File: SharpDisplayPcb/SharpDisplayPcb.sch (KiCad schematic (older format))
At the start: 1 part, among them J1 Conn_01x08_Female

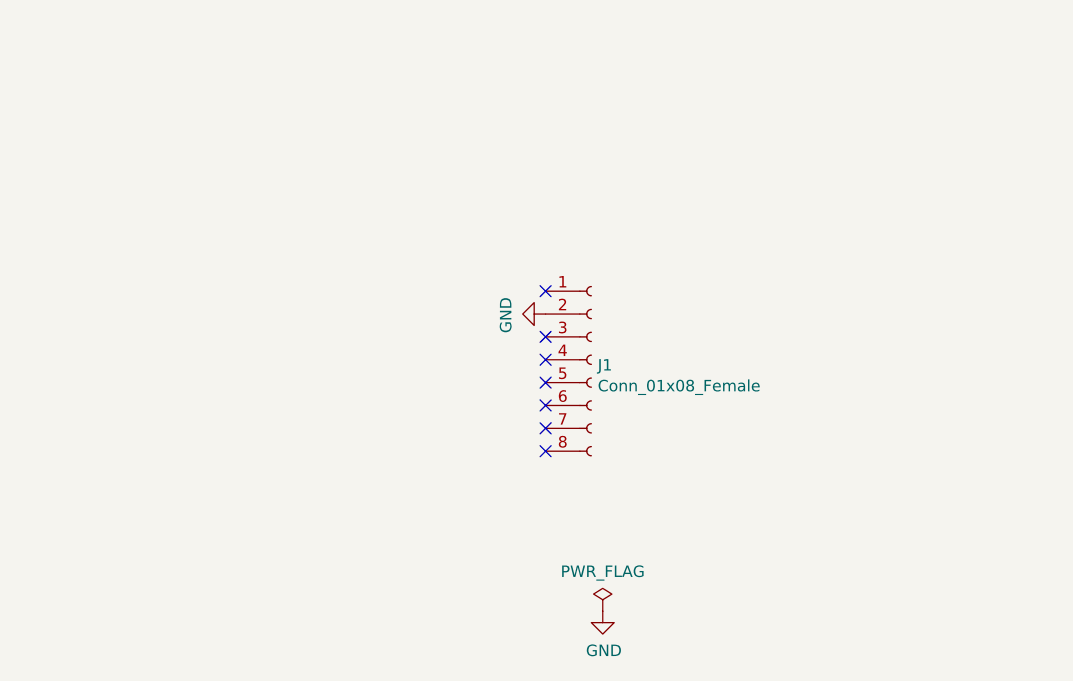
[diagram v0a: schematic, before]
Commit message: Completed schematics, initial PCB layout
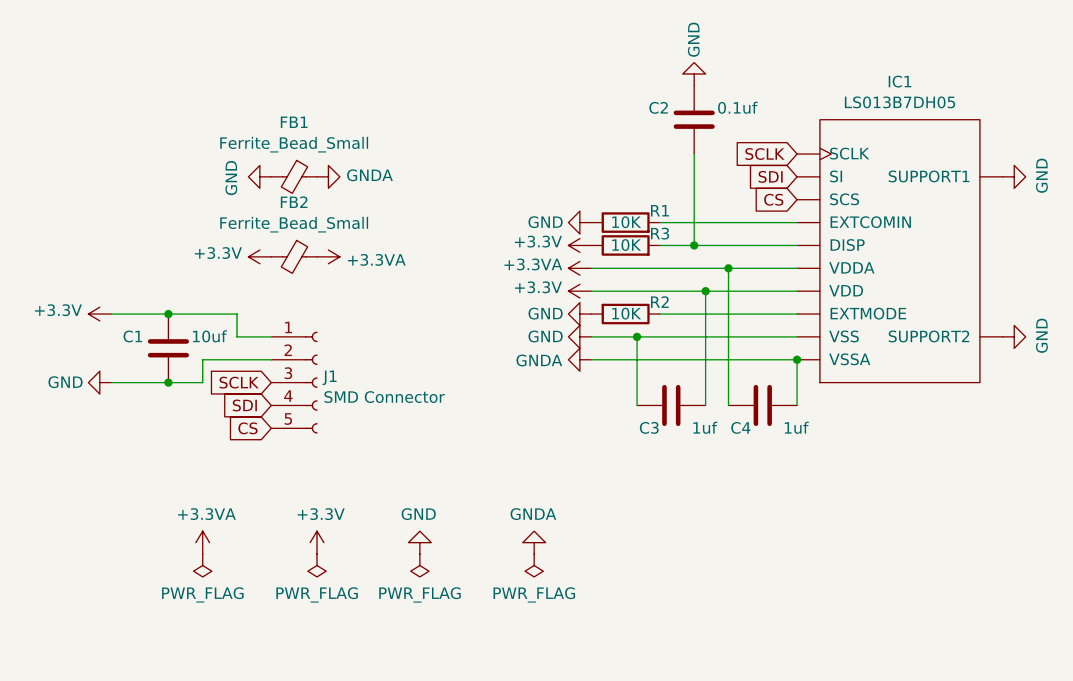
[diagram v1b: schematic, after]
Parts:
- removed J1: Conn_01x08_Female, Connector_PinHeader_2.54mm:PinHeader_1x08_P2.54mm_Vertical, symbol Connector:Conn_01x08_Female
- added C1: 10uf, Capacitor_SMD:C_0805_2012Metric_Pad1.18x1.45mm_HandSolder, symbol Device:C
- added C2: 0.1uf, Capacitor_SMD:C_0805_2012Metric_Pad1.18x1.45mm_HandSolder, symbol Device:C
- added C3, C4: 1uf, Capacitor_SMD:C_0805_2012Metric_Pad1.18x1.45mm_HandSolder, symbol Device:C
- added FB1, FB2: Ferrite_Bead_Small, Inductor_SMD:L_0805_2012Metric_Pad1.15x1.40mm_HandSolder, symbol Device:Ferrite_Bead_Small
- added IC1: LS013B7DH05, SharpDisplay:FPC_10PIN_52892-1033, symbol SharpDisplayPcb:LS013B7DH05
- added J1: SMD Connector, Connector_PinHeader_2.54mm:PinHeader_1x05_P2.54mm_Vertical, symbol Connector:Conn_01x05_Female
- added R1, R2, R3: 10K, Resistor_SMD:R_0805_2012Metric_Pad1.20x1.40mm_HandSolder, symbol Device:R
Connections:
- net GND: now also C1.2, C2.1, C3.1, FB1.2, IC1.SUPPORT1, IC1.SUPPORT2, IC1.VSS, J1.2 (Pin_2), R1.1, R2.2
- new net: C2.2, IC1.DISP, R3.2
- new net: IC1.EXTCOMIN, R1.2
- new net: IC1.EXTMODE, R2.1
- new net +3.3VA: C4.1, FB2.1, IC1.VDDA
- new net +3V3: C1.1, C3.2, FB2.2, IC1.VDD, J1.1 (Pin_1), R3.1
- new net CS: IC1.SCS, J1.5 (Pin_5)
- new net GNDA: C4.2, FB1.1, IC1.VSSA
- new net SCLK: IC1.SCLK, J1.3 (Pin_3)
- new net SDI: IC1.SI, J1.4 (Pin_4)
- no-connect marks 7 -> 0

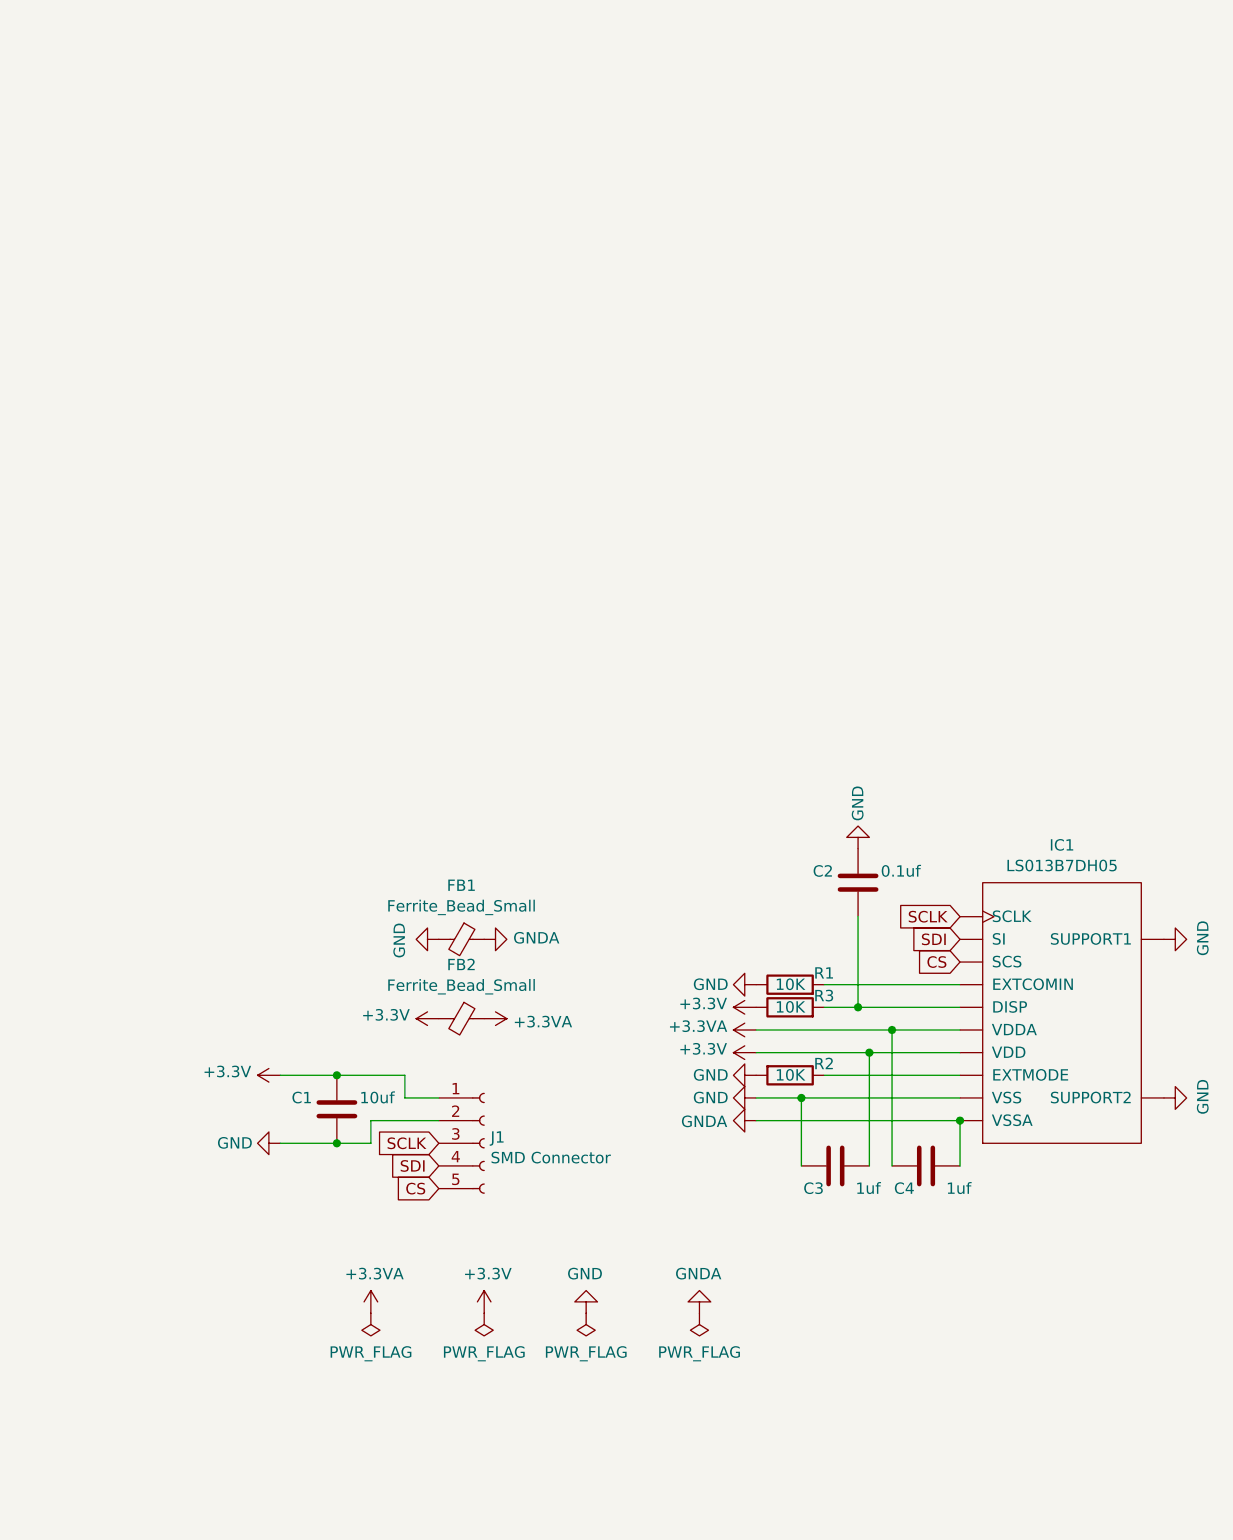
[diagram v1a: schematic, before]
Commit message: Add DISP jumper, to disable pull-up resistor
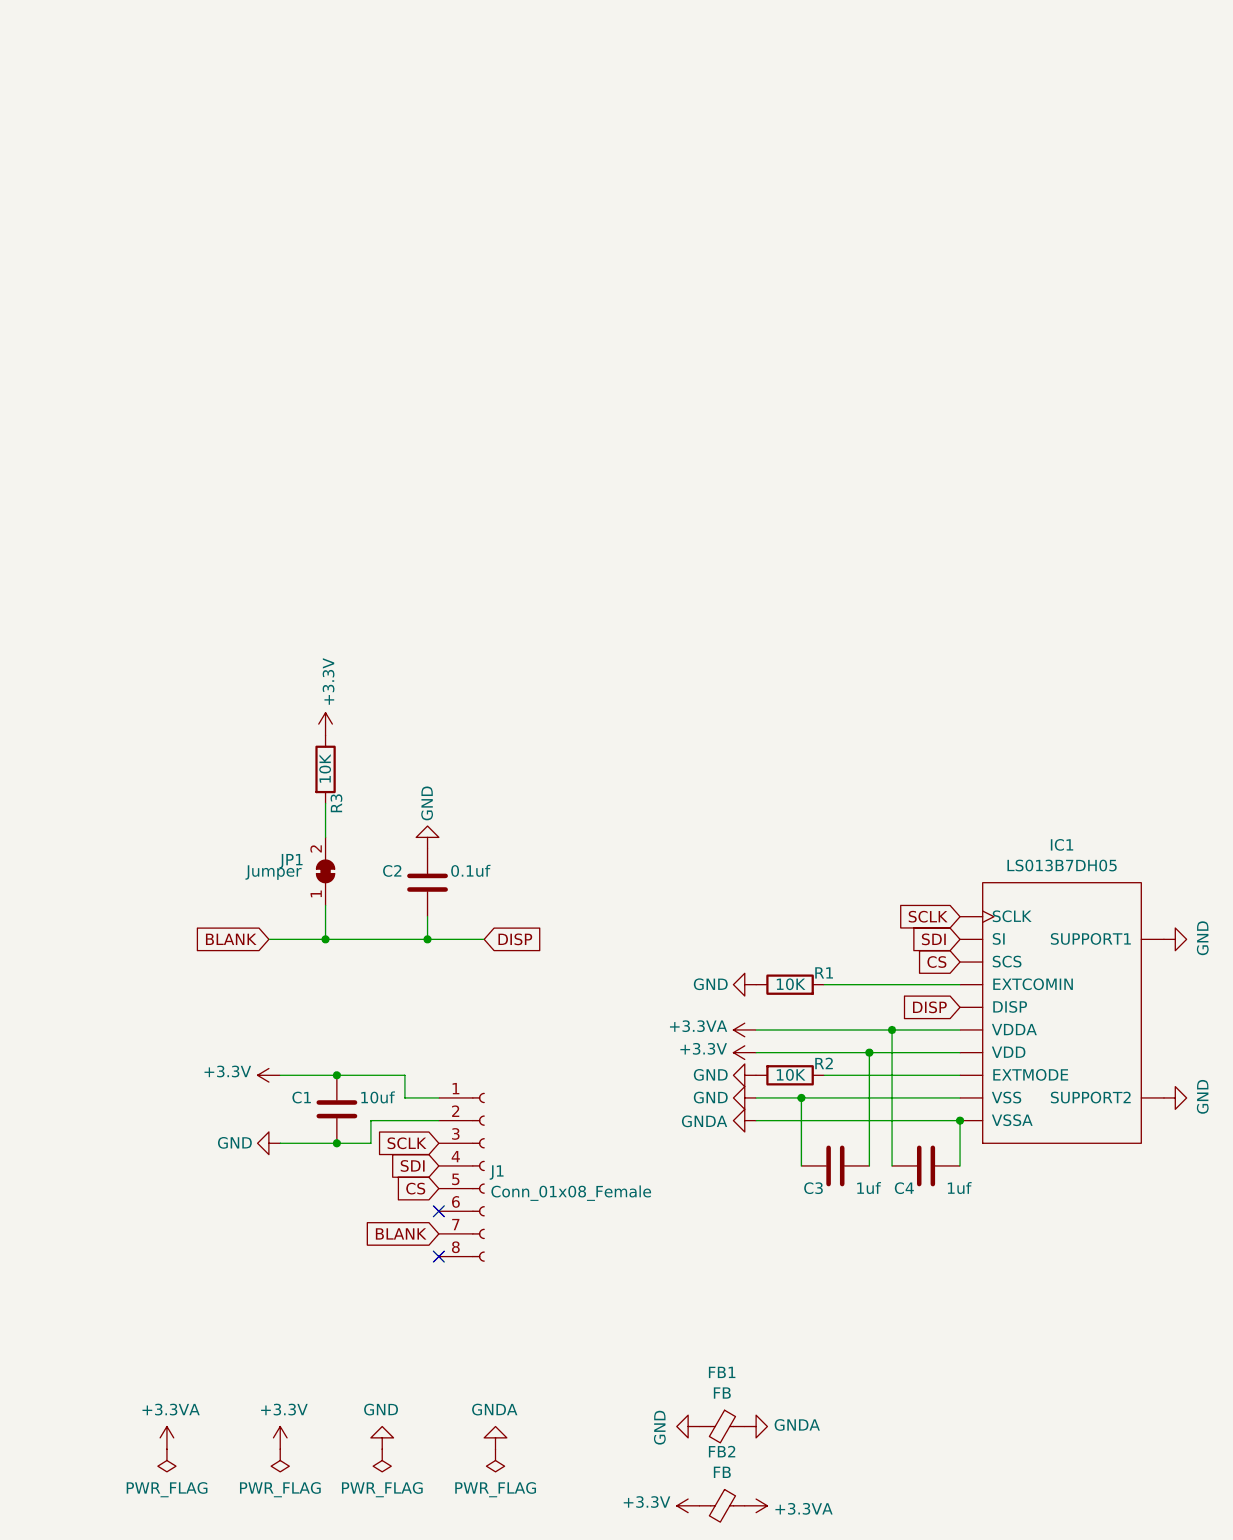
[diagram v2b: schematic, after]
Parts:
- removed J1: SMD Connector, Connector_PinHeader_2.54mm:PinHeader_1x05_P2.54mm_Vertical, symbol Connector:Conn_01x05_Female
- added J1: Conn_01x08_Female, Connector_PinHeader_2.54mm:PinHeader_1x08_P2.54mm_Vertical, symbol Connector:Conn_01x08_Female
- added JP1: Jumper, Jumper:SolderJumper-2_P1.3mm_Bridged_Pad1.0x1.5mm, symbol Jumper:SolderJumper_2_Bridged
- FB1, FB2: value Ferrite_Bead_Small -> FB
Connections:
- net +3V3: now also J1.1 (Pin_1)
- net CS: now also J1.5 (Pin_5)
- net GND: now also J1.2 (Pin_2)
- net SCLK: now also J1.3 (Pin_3)
- net SDI: now also J1.4 (Pin_4)
- net BLANK: now reaches C2.2, IC1.DISP
- net BLANK: now also J1.7 (Pin_7), JP1.1 (A); no longer R3.2
- new net: JP1.2 (B), R3.2
- no-connect marks 0 -> 2
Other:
- moved on the sheet: C2, FB1, FB2, R3

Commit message: Remove pull-down resistors, adjust layout
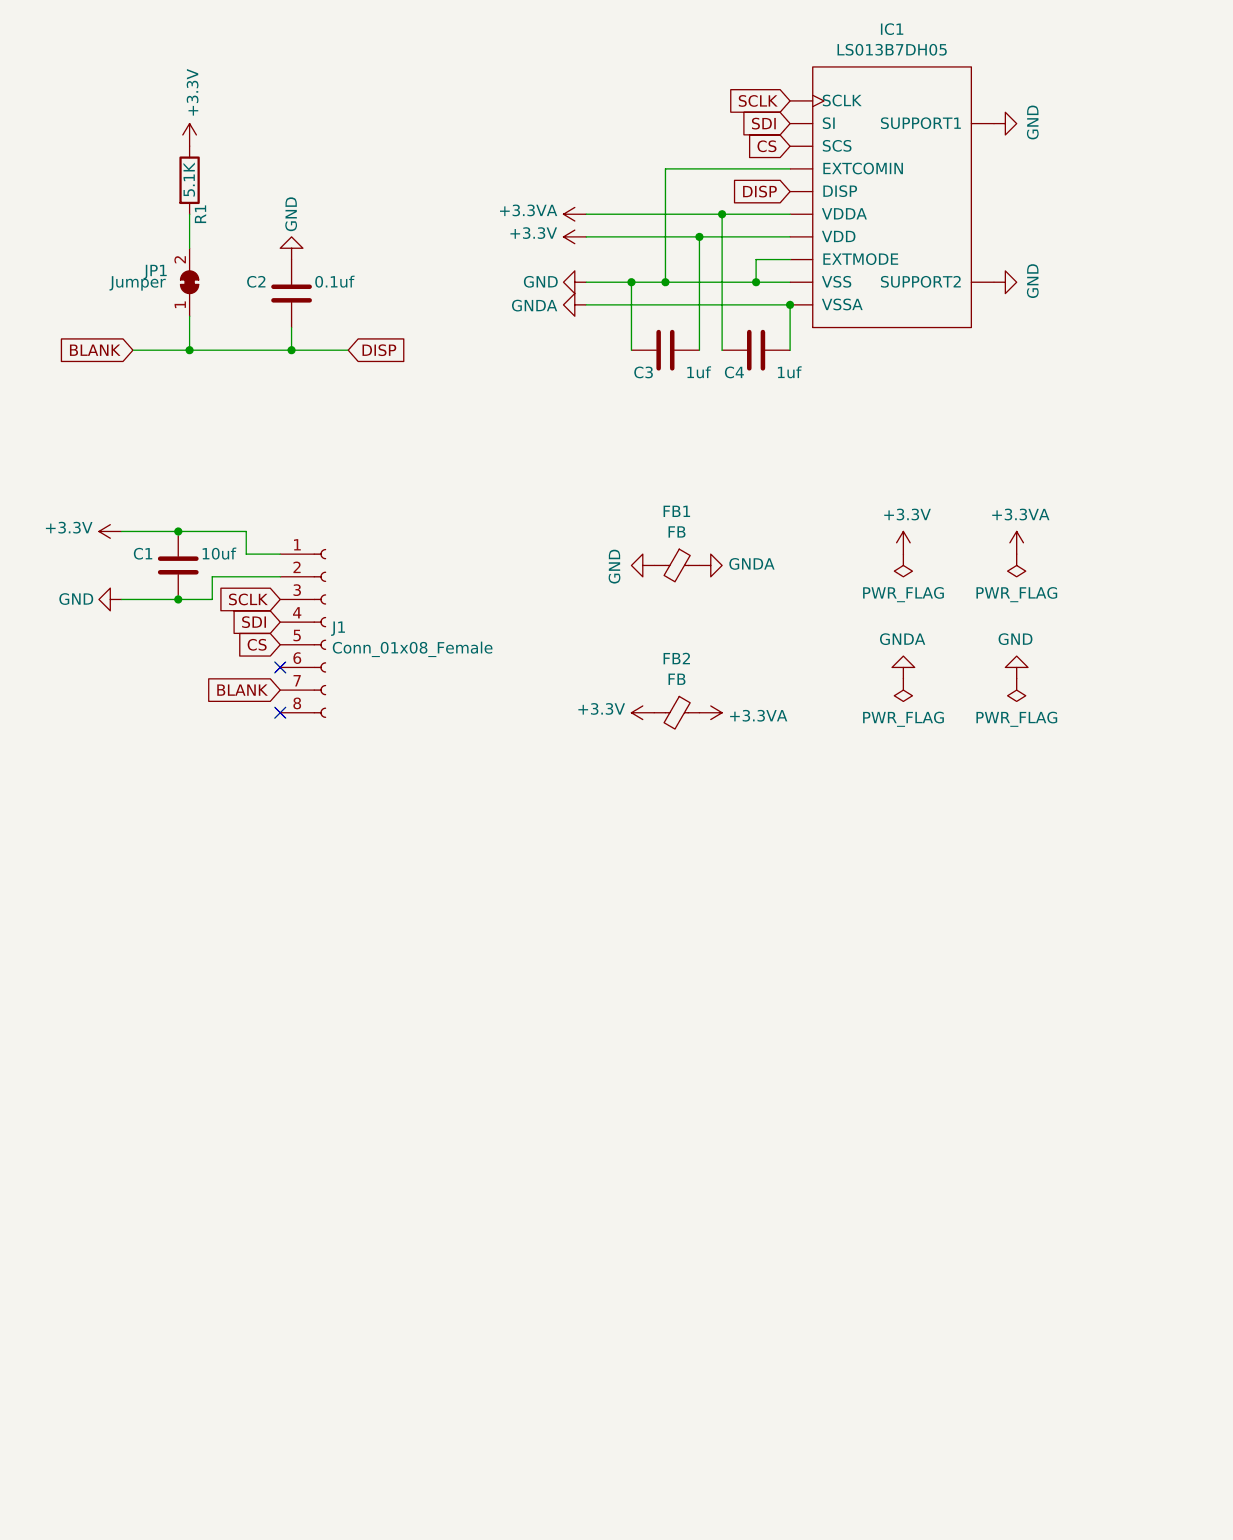
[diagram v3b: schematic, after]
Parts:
- removed R1, R2: 10K, Resistor_SMD:R_0805_2012Metric_Pad1.20x1.40mm_HandSolder, symbol Device:R
- R1: renamed from R3; value 10K -> 5.1K
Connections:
- net GND: now also IC1.EXTCOMIN, IC1.EXTMODE
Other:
- moved on the sheet: C1, C2, C3, C4, FB1, FB2, IC1, J1, JP1, R1

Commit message: Replace ZIF part, move components out of ZIF footprint
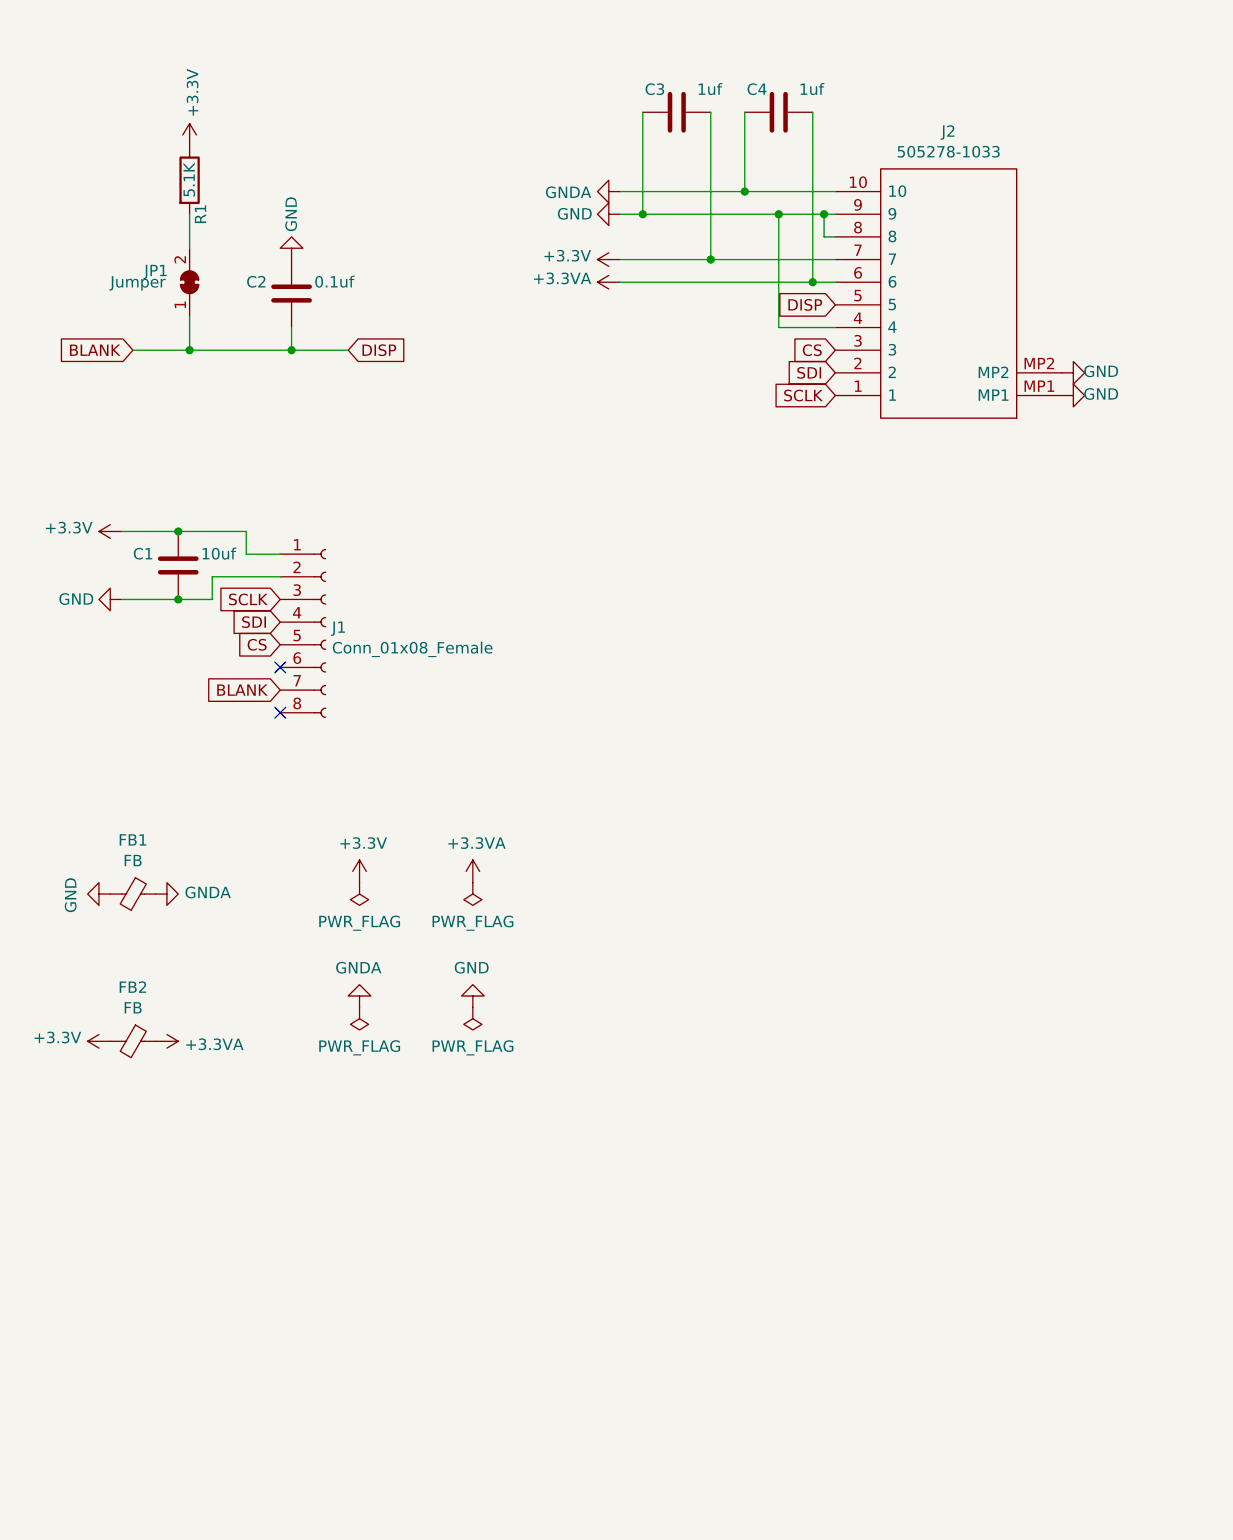
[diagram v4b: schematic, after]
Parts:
- removed IC1: LS013B7DH05, SharpDisplay:FPC_10PIN_52892-1033, symbol SharpDisplayPcb:LS013B7DH05
- added J2: 505278-1033, SharpDisplay:5052781033, symbol SharpDisplayPcb:505278-1033
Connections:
- net +3.3VA: now also C4.2, J2.6; no longer C4.1
- net +3V3: now also J2.7
- net BLANK: now also J2.5
- net CS: now also J2.3
- net GND: now also J2.4, J2.8, J2.9, J2.MP1, J2.MP2
- net GNDA: now also C4.1, J2.10; no longer C4.2
- net SCLK: now also J2.1
- net SDI: now also J2.2
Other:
- moved on the sheet: C3, C4, FB1, FB2
